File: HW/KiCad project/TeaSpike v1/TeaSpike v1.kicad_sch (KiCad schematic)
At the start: 23 parts, among them U1 TP4056, U2 PowerBoost

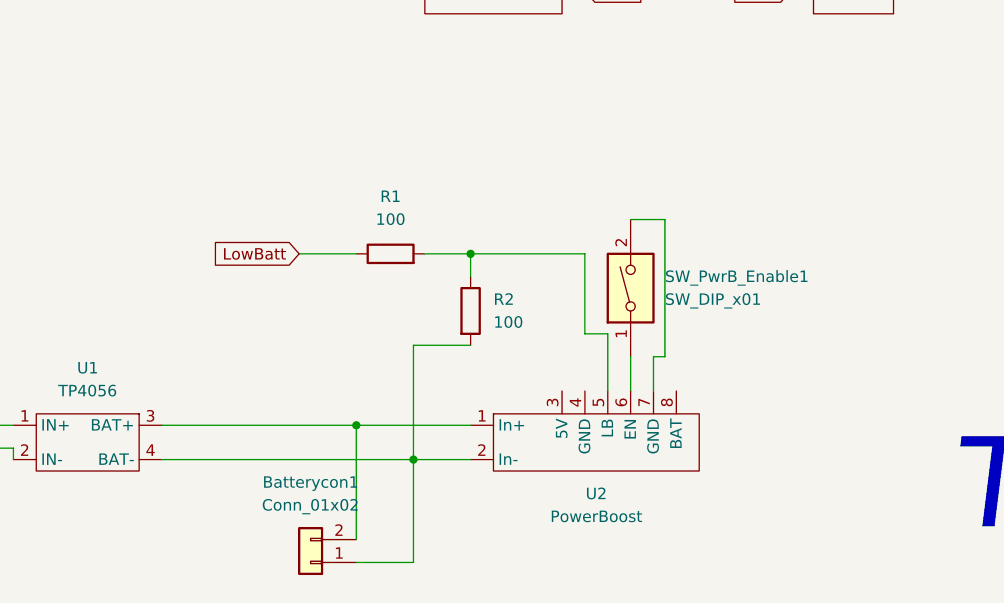
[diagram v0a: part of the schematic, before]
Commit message: Modificado circuito alimentación. Añadido aviso low bat.
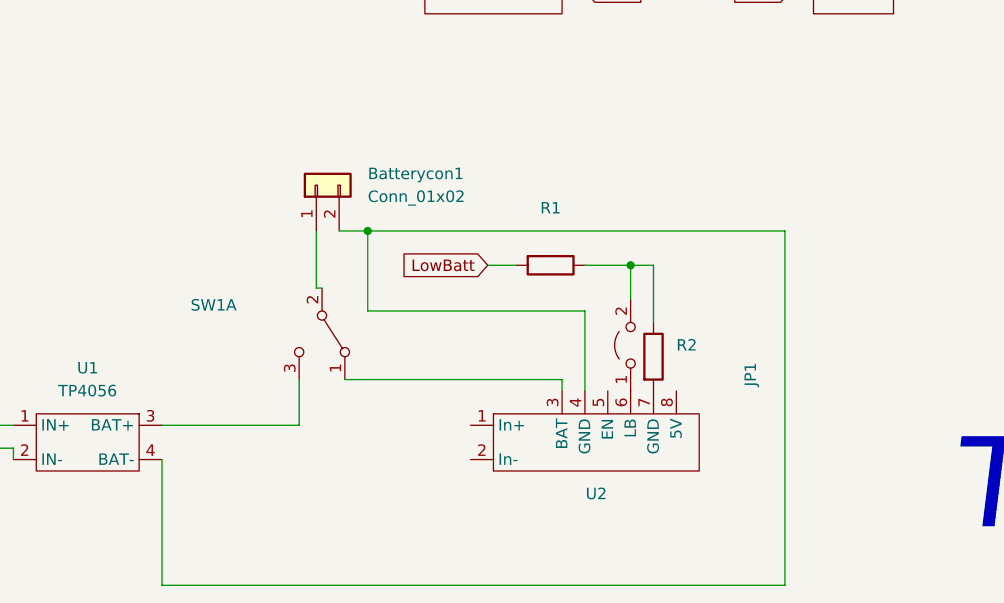
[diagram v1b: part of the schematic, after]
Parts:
- removed SW_PwrB_Enable1: SW_DIP_x01, TerminalBlock:TerminalBlock_bornier-2_P5.08mm, symbol Switch:SW_DIP_x01
- added JP1: (no value), symbol Jumper:Jumper_2_Open
- added SW1: (no value), symbol Switch:SW_DPDT_x2
- R1, R2: value 100 -> (none); footprint Resistor_THT:R_Axial_DIN0207_L6.3mm_D2.5mm_P7.62mm_Horizontal -> (none)
- U2: value PowerBoost -> (none); footprint TeaSpike_Periferalls:PowerBoost -> (none)
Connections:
- net LowBatt: now also R1.2; no longer R1.1
- net at U2.3 (BAT): now also SW1.1 (A)
- net at U2.4 (GND): now also Batterycon1.2 (Pin_2), U1.4 (BAT-)
- net at U2.6 (LB): now also JP1.1 (A)
- net at U2.7 (GND): now also R2.2
- new net: JP1.2 (B), R1.1, R2.1
- new net: SW1.3 (C), U1.3 (BAT+)
- new net: Batterycon1.1 (Pin_1), SW1.2 (B)
- now unconnected: U2.1 (In+), U2.2 (In-), U2.5 (LB)
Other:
- moved on the sheet: Batterycon1

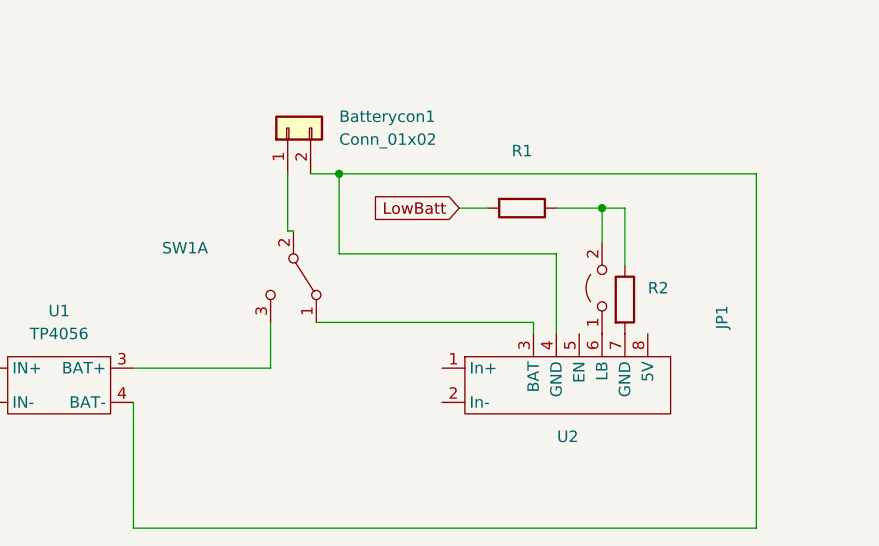
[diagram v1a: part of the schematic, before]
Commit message: Versión tras revisión de Marina. Creado SpectraDSN. Falta routear las pistas
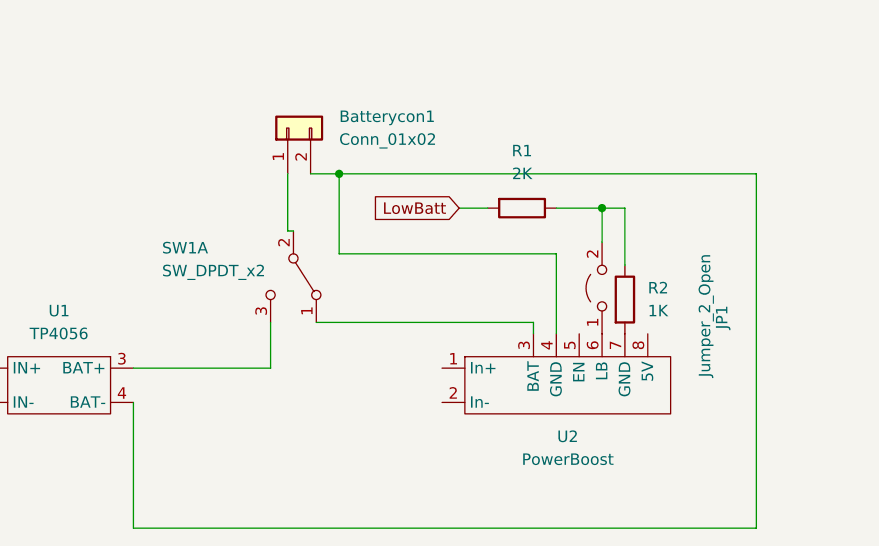
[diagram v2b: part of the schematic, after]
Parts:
- JP1: value (none) -> Jumper_2_Open; footprint (none) -> Connector_PinHeader_2.54mm:PinHeader_1x02_P2.54mm_Vertical
- R1: value (none) -> 2K; footprint (none) -> Resistor_THT:R_Axial_DIN0207_L6.3mm_D2.5mm_P7.62mm_Horizontal
- R2: value (none) -> 1K; footprint (none) -> Resistor_THT:R_Axial_DIN0207_L6.3mm_D2.5mm_P7.62mm_Horizontal
- SW1: value (none) -> SW_DPDT_x2; footprint (none) -> Button_Switch_THT:SW_CuK_JS202011AQN_DPDT_Angled
- U2: value (none) -> PowerBoost; footprint (none) -> TeaSpike_Periferalls:PowerBoost
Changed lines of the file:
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@@
     (in_bom yes) (on_board yes) (fields_autoplaced)
     (property "Reference" "U2" (id 0) (at 137.16 175.26 0))
-    (property "Value" "" (id 1) (at 137.16 177.8 0))
-    (property "Footprint" "" (id 2) (at 125.73 161.29 0)
+    (property "Value" "PowerBoost" (id 1) (at 137.16 177.8 0))
+    (property "Footprint" "TeaSpike_Periferalls:PowerBoost" (id 2) (at 125.73 161.29 0)
       (effects (font (size 1.27 1.27)) hide)
     )
@@
       (effects (font (size 1.27 1.27)) (justify right))
     )
-    (property "Value" "" (id 1) (at 152.4 154.94 0)
-      (effects (font (size 1.27 1.27)) (justify right))
-    )
-    (property "Footprint" "" (id 2) (at 140.97 158.75 0)
+    (property "Value" "Jumper_2_Open" (id 1) (at 152.4 154.94 0)
+      (effects (font (size 1.27 1.27)) (justify right))
+    )
+    (property "Footprint" "Connector_PinHeader_2.54mm:PinHeader_1x02_P2.54mm_Vertical" (id 2) (at 140.97 158.75 0)
       (effects (font (size 1.27 1.27)) hide)
     )
@@
       (effects (font (size 1.27 1.27)) (justify left))
     )
-    (property "Value" "" (id 1) (at 146.05 161.2899 0)
-      (effects (font (size 1.27 1.27)) (justify left))
-    )
-    (property "Footprint" "" (id 2) (at 141.732 160.02 90)
+    (property "Value" "1K" (id 1) (at 146.05 161.2899 0)
+      (effects (font (size 1.27 1.27)) (justify left))
+    )
+    (property "Footprint" "Resistor_THT:R_Axial_DIN0207_L6.3mm_D2.5mm_P7.62mm_Horizontal" (id 2) (at 141.732 160.02 90)
       (effects (font (size 1.27 1.27)) hide)
     )
@@
     (in_bom yes) (on_board yes) (fields_autoplaced)
     (property "Reference" "R1" (id 0) (at 132.08 143.51 90))
-    (property "Value" "" (id 1) (at 132.08 146.05 90))
-    (property "Footprint" "" (id 2) (at 132.08 148.082 90)
+    (property "Value" "2K" (id 1) (at 132.08 146.05 90))
+    (property "Footprint" "Resistor_THT:R_Axial_DIN0207_L6.3mm_D2.5mm_P7.62mm_Horizontal" (id 2) (at 132.08 148.082 90)
       (effects (font (size 1.27 1.27)) hide)
     )
@@
       (effects (font (size 1.27 1.27)) (justify left))
     )
-    (property "Value" "" (id 1) (at 92.075 156.845 90)
-      (effects (font (size 1.27 1.27)) (justify left))
-    )
-    (property "Footprint" "" (id 2) (at 106.68 157.48 0)
-      (effects (font (size 1.27 1.27)) hide)
-    )
+    (property "Value" "SW_DPDT_x2" (id 1) (at 92.075 156.845 90)
+      (effects (font (size 1.27 1.27)) (justify left))
+    )
+    (property "Footprint" "Button_Switch_THT:SW_CuK_JS202011AQN_DPDT_Angled" (id 2) (at 106.68 157.48 0)
+      (effects (font (size 1.27 1.27)) hide)
+    )

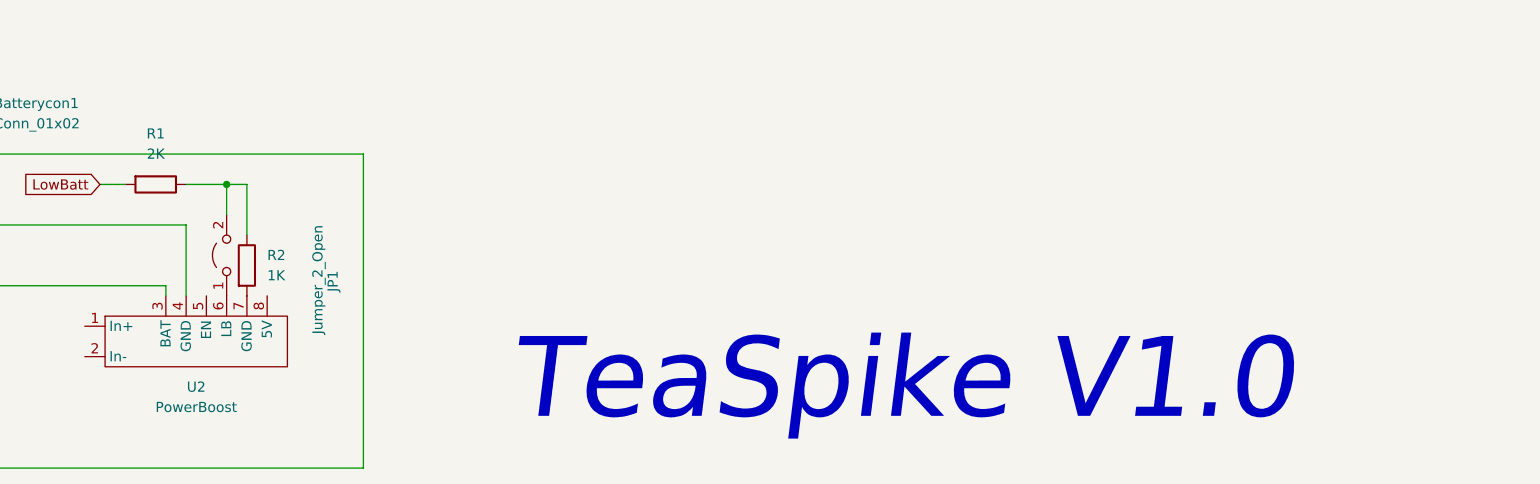
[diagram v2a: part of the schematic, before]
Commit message: Corregido ancho de pista
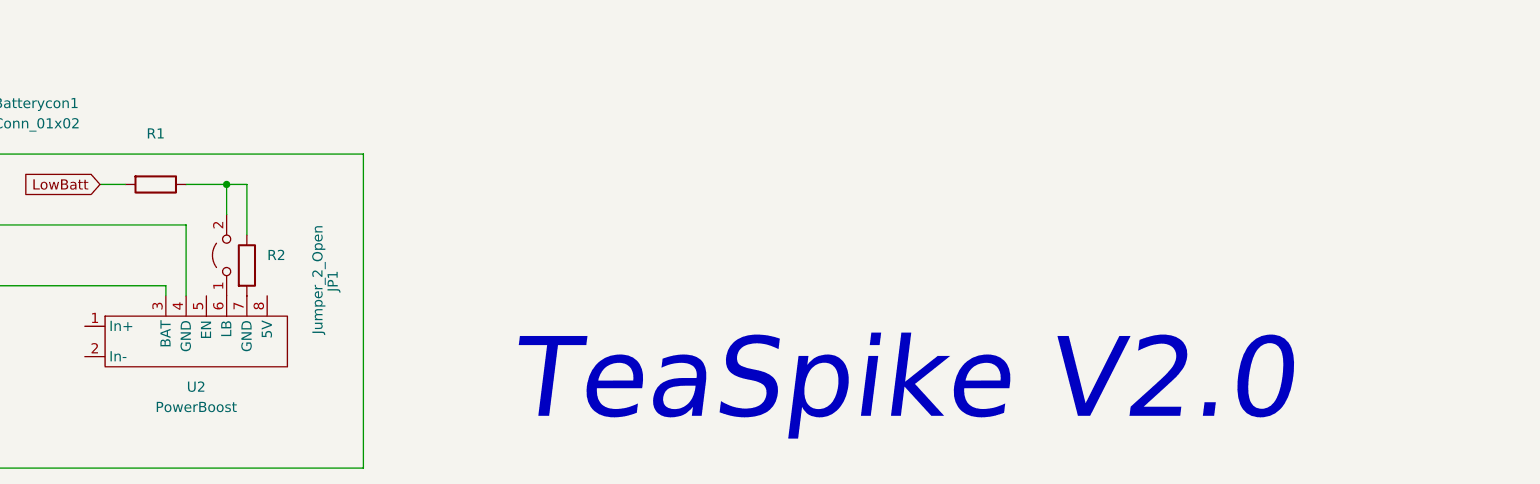
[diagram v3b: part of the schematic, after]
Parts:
- R1: value 2K -> (none)
- R2: value 1K -> (none)
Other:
- note added: "TeaSpike V2.0"
- note removed: "TeaSpike V1.0"
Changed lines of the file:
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@@
     )
   )
-  (text "TeaSpike V1.0" (at 176.53 180.34 0)
+  (text "TeaSpike V2.0" (at 176.53 180.34 0)
     (effects (font (size 10.0076 10.0076) italic) (justify left bottom))
   )
@@
       (effects (font (size 1.27 1.27)) (justify left))
     )
-    (property "Value" "1K" (id 1) (at 146.05 161.2899 0)
+    (property "Value" "" (id 1) (at 146.05 161.2899 0)
       (effects (font (size 1.27 1.27)) (justify left))
     )
@@
     (in_bom yes) (on_board yes) (fields_autoplaced)
     (property "Reference" "R1" (id 0) (at 132.08 143.51 90))
-    (property "Value" "2K" (id 1) (at 132.08 146.05 90))
+    (property "Value" "" (id 1) (at 132.08 146.05 90))
     (property "Footprint" "Resistor_THT:R_Axial_DIN0207_L6.3mm_D2.5mm_P7.62mm_Horizontal" (id 2) (at 132.08 148.082 90)
       (effects (font (size 1.27 1.27)) hide)
@@
     )
     (path "/c9ba50c9-67b0-4394-8e9d-a1abf78b9106"
-      (reference "R1") (unit 1) (value "2K") (footprint "Resistor_THT:R_Axial_DIN0207_L6.3mm_D2.5mm_P7.62mm_Horizontal")
+      (reference "R1") (unit 1) (value "1K") (footprint "Resistor_THT:R_Axial_DIN0207_L6.3mm_D2.5mm_P7.62mm_Horizontal")
     )
     (path "/aecd2b42-4343-4526-8b9d-8ca85518449b"
-      (reference "R2") (unit 1) (value "1K") (footprint "Resistor_THT:R_Axial_DIN0207_L6.3mm_D2.5mm_P7.62mm_Horizontal")
+      (reference "R2") (unit 1) (value "2K") (footprint "Resistor_THT:R_Axial_DIN0207_L6.3mm_D2.5mm_P7.62mm_Horizontal")
     )
     (path "/00000000-0000-0000-0000-00006241d575"
